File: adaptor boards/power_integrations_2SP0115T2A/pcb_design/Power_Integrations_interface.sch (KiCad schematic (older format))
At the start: 20 parts, among them J1 GATE_DRIVER_CONN_U, J10 current sensor, J2 GATE_DRIVER_CONN_V, J3 GATE_DRIVER_CONN_W, J4 VBUS, J5 CONN-100MIL-F-1x2, J6 CONN-100MIL-M-1x4, J8 current sensor, J9 current sensor, P1 2SP0115T_conector, P2 2SP0115T_conector, P3 2SP0115T_conector, U1 LM1117IMP-v.v

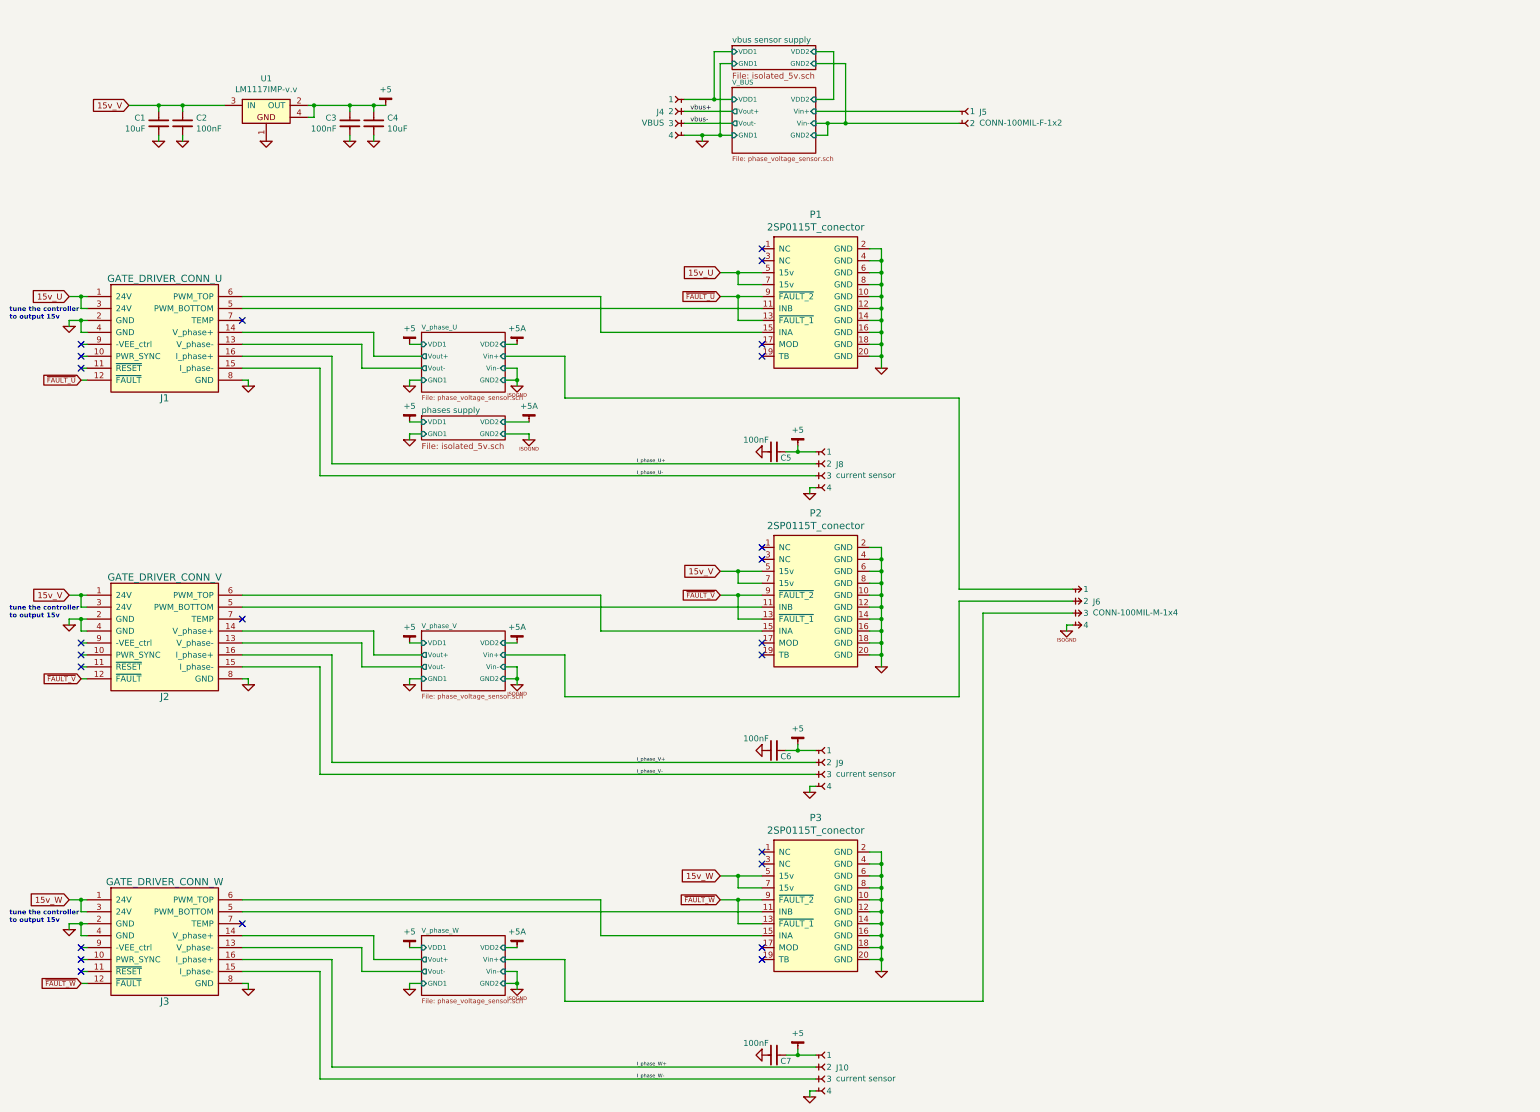
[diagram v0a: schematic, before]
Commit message: Fix swapped differential signals in the interface board
Signed-off-by: Marcos Chaparro <mchaparro@paltatech.com>
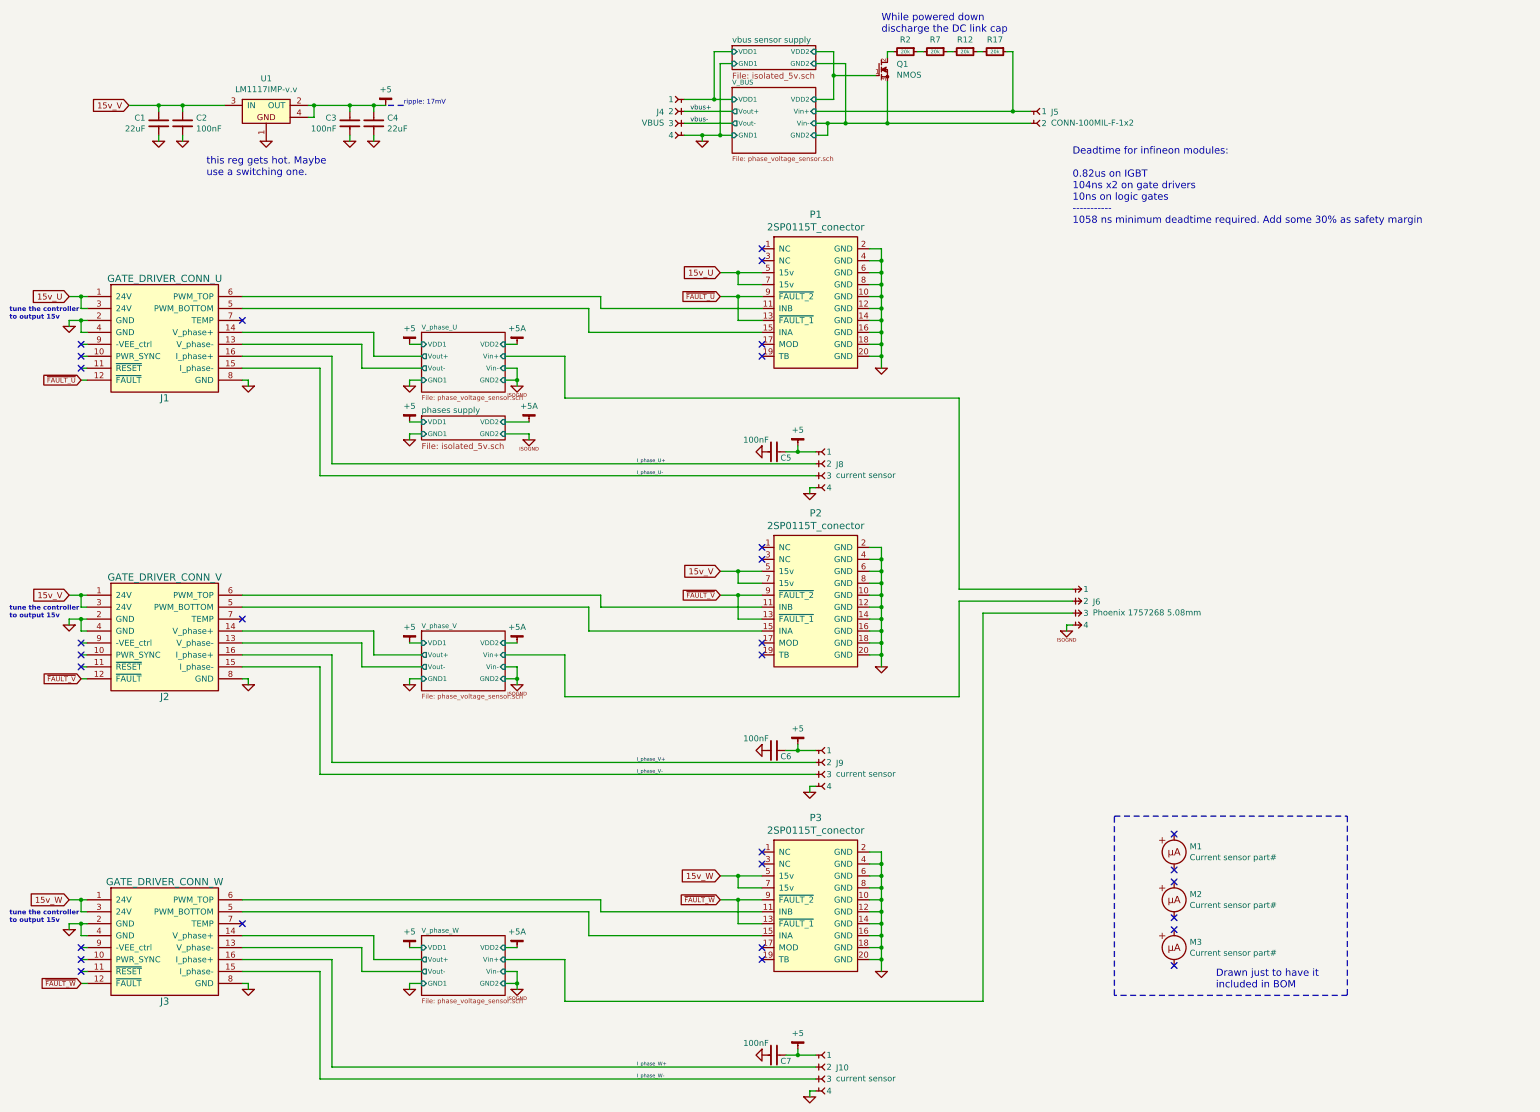
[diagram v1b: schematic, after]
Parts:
- added M1, M2, M3: Current sensor part#, symbol UAMMETER
- added Q1: NMOS, symbol NMOS
- added R12, R17, R2, R7: 20k, IPC7351-Nominal:RESC6432X70, symbol R-2512
- C1, C4: value 10uF -> 22uF; MFR (none) -> TDK Corporation; MPN (none) -> C2012X5R1V226M125AC; SPN (none) -> 445-14428-1-ND; SPR (none) -> Digikey
- C2, C3, C5, C6, C7: MFR (none) -> Murata Electronics North America; MPN (none) -> GRM188R71E104KA01D; SPN (none) -> 490-1524-1-ND; SPR (none) -> Digikey
- J1, J2, J3: MPN 67997-216HLF -> 87606-308LF; SPN 609-3238-ND -> 609-3554-ND
- J10, J4, J8, J9: MFR (none) -> JST Sales America Inc.; MPN (none) -> B4B-PH-K-S(LF)(SN); SPN (none) -> 455-1706-ND; SPR (none) -> Digikey
- J5: MFR (none) -> Phoenix Contact; MPN (none) -> 1923869; SPN (none) -> 277-6570-ND; SPR (none) -> Digikey
- J6: value CONN-100MIL-M-1x4 -> Phoenix 1757268 5.08mm; MFR (none) -> Phoenix Contact; MPN (none) -> 1757268; SPN (none) -> 277-1108-ND; SPR (none) -> Digikey
- P1: MFR (none) -> Amphenol FCI; SPN (none) -> 609-1776-ND; SPR (none) -> Digikey
- P2, P3: MFR (none) -> Amphenol FCI; MPN (none) -> 75869-104LF; SPN (none) -> 609-1776-ND; SPR (none) -> Digikey
- U1: MFR (none) -> ON Semiconductor; MPN (none) -> NCV1117ST50T3G; SPN (none) -> NCV1117ST50T3GOSCT-ND; SPR (none) -> Digikey
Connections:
- net V_BUS/GND2: now also Q1.3 (S)
- net V_BUS/VDD2: now also Q1.1 (G)
- net V_BUS/Vin+: now also R17.1
- net at J1.5 (PWM_BOTTOM): now also P1.15 (INA); no longer P1.11 (INB)
- net at J1.6 (PWM_TOP): now also P1.11 (INB); no longer P1.15 (INA)
- net at J2.5 (PWM_BOTTOM): now also P2.15 (INA); no longer P2.11 (INB)
- net at J2.6 (PWM_TOP): now also P2.11 (INB); no longer P2.15 (INA)
- net at J3.5 (PWM_BOTTOM): now also P3.15 (INA); no longer P3.11 (INB)
- net at J3.6 (PWM_TOP): now also P3.11 (INB); no longer P3.15 (INA)
- new net: R2.1, R7.2
- new net: Q1.2 (D), R2.2
- new net: R12.2, R7.1
- new net: R12.1, R17.2
- no-connect marks 24 -> 30
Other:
- note added: "Deadtime for infineon modules:\n\n0.82us on IGBT\n104ns x2 on gate drivers\n10ns on logic gates\n-----------\n1058 ns minimum deadtime required. Add some 30% as safety margin"
- note added: "Drawn just to have it\nincluded in BOM"
- note added: "While powered down\ndischarge the DC link cap"
- note added: "ripple: 17mV"
- note added: "this reg gets hot. Maybe\nuse a switching one."
- moved on the sheet: J5
